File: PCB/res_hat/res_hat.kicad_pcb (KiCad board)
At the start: 2 copper layers, 85 x 56 mm, 55 parts, among them IC1 MCP4725A0T-E_CH, IC2 MCP4725A0T-E_CH, IC3 UCC27324D, J1 Conn_02x20_Odd_Even, J10 Conn_01x02, J11 Jack-DC, J2 Conn_02x04_Odd_Even, J3 Conn_01x03, J4 Conn_01x06, J5 Conn_Coaxial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

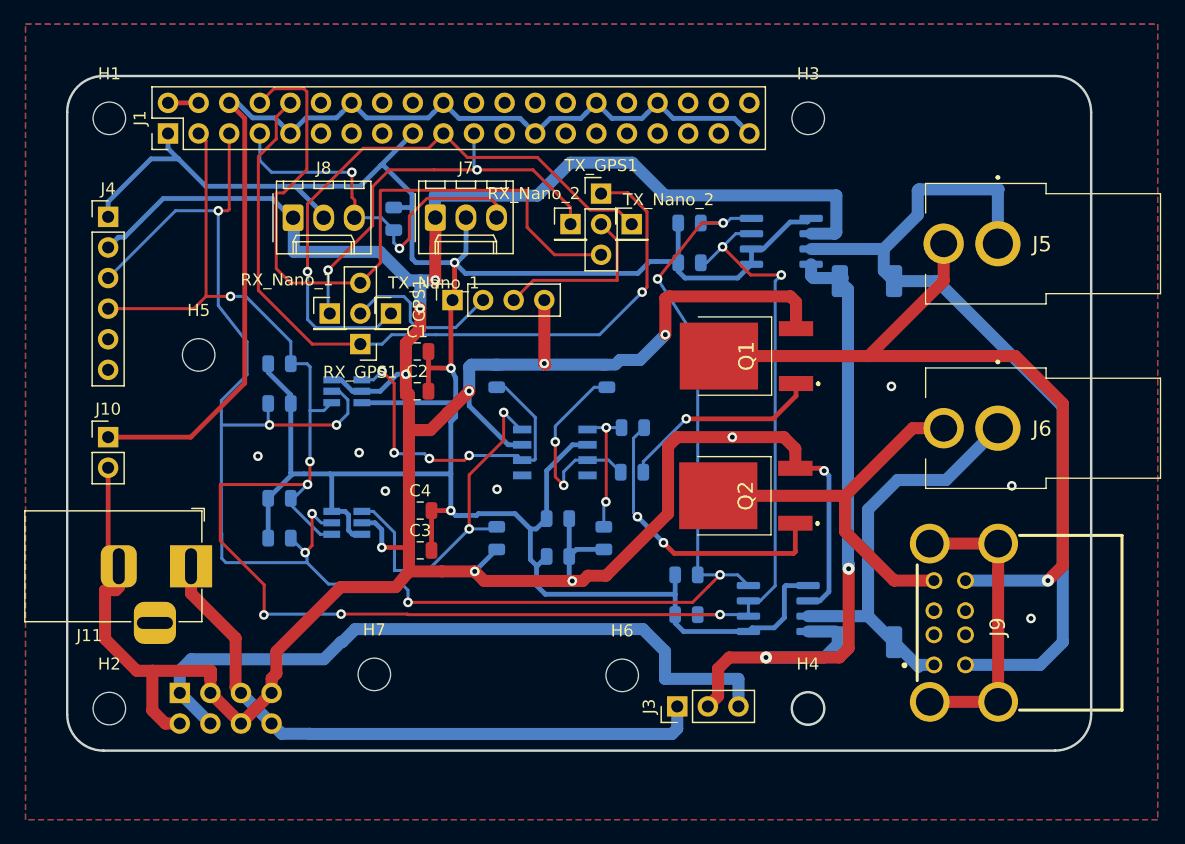
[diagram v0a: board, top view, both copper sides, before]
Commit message: update/add LCSC ref and create fab file
bug for Res_hat with JLCPCB site
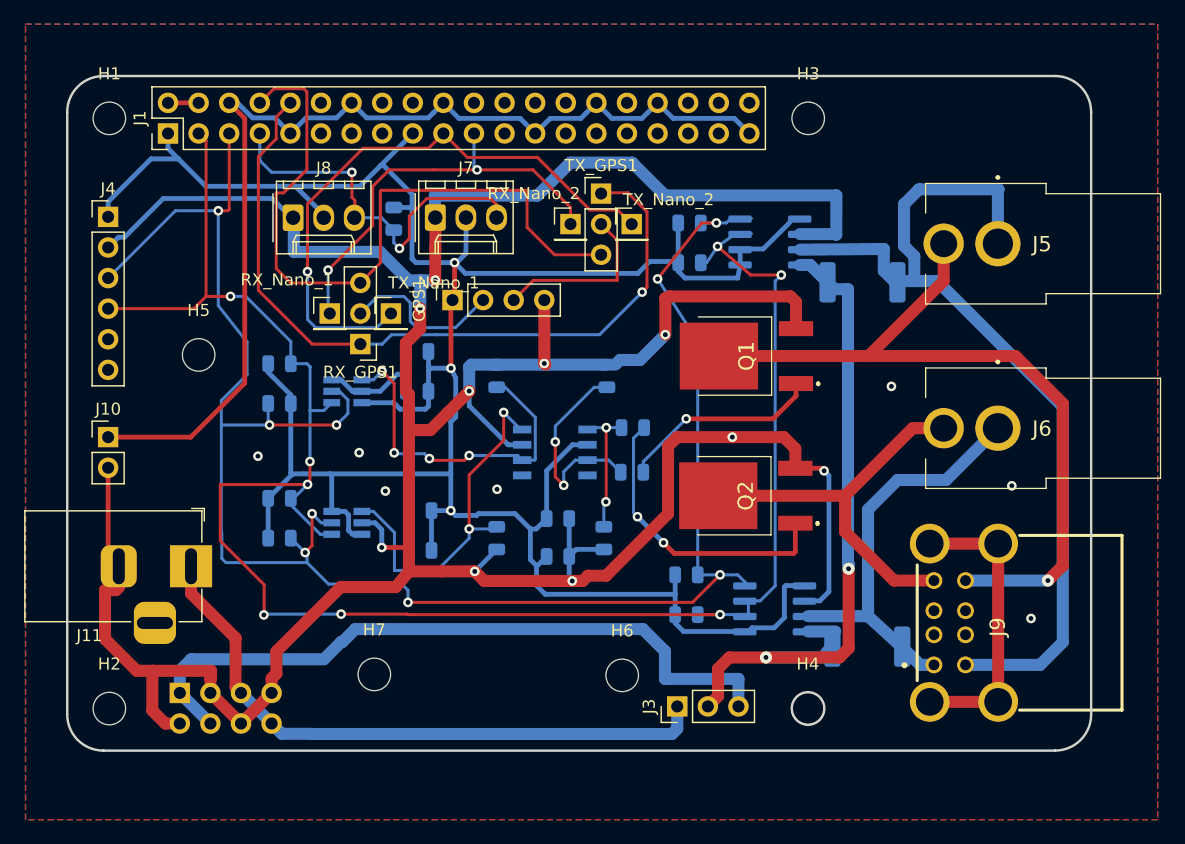
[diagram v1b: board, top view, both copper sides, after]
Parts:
- C1, C2, C3, C4: moved to B.Cu
- R11, R13: value 0.02 -> 0.02 1W; footprint Resistor_SMD:R_2010_5025Metric -> Resistor_SMD:R_2512_6332Metric
- moved U1 0.95 mm to (120.2, 112.1)
- moved R11 0.39 mm to (127.9, 115.4)
- moved R13 0.37 mm to (128.3, 145.7)
- moved U2 0.30 mm to (120.6, 142.5)
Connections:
- IC3 pad 1: (no net) -> Net-(IC3-Pad1)
- IC3 pad 8: (no net) -> Net-(IC3-Pad8)
- J1 pad 11: (no net) -> Net-(J1-Pad11)
- J1 pad 12: (no net) -> Net-(J1-Pad12)
- J1 pad 13: (no net) -> Net-(J1-Pad13)
- J1 pad 15: (no net) -> Net-(J1-Pad15)
- J1 pad 16: (no net) -> Net-(J1-Pad16)
- J1 pad 18: (no net) -> Net-(J1-Pad18)
- J1 pad 22: (no net) -> Net-(J1-Pad22)
- J1 pad 23: (no net) -> Net-(J1-Pad23)
- J1 pad 24: (no net) -> Net-(J1-Pad24)
- J1 pad 26: (no net) -> Net-(J1-Pad26)
- J1 pad 27: (no net) -> Net-(J1-Pad27)
- J1 pad 28: (no net) -> Net-(J1-Pad28)
- J1 pad 29: (no net) -> Net-(J1-Pad29)
- J1 pad 31: (no net) -> Net-(J1-Pad31)
- J1 pad 32: (no net) -> Net-(J1-Pad32)
- J1 pad 33: (no net) -> Net-(J1-Pad33)
- J1 pad 35: (no net) -> Net-(J1-Pad35)
- J1 pad 36: (no net) -> Net-(J1-Pad36)
- J1 pad 37: (no net) -> Net-(J1-Pad37)
- J1 pad 38: (no net) -> Net-(J1-Pad38)
- J1 pad 40: (no net) -> Net-(J1-Pad40)
- J4 pad 5: (no net) -> /CSB
- J4 pad 6: (no net) -> /SDO
- J9 pad 2: (no net) -> Net-(J9-Pad2)
- J9 pad 3: (no net) -> Net-(J9-Pad3)
- J9 pad 6: (no net) -> Net-(J9-Pad6)
- J9 pad 7: (no net) -> Net-(J9-Pad7)
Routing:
- net +3V3: track 226.1 -> 221.6 mm
- net Net-(J5-Pad1): track 73.1 -> 76.3 mm
- net GND: track 299.1 -> 300.2 mm, vias 18 -> 17
- net /SCL: track 159.5 -> 158.9 mm
- net VD: track 58.4 -> 57.9 mm

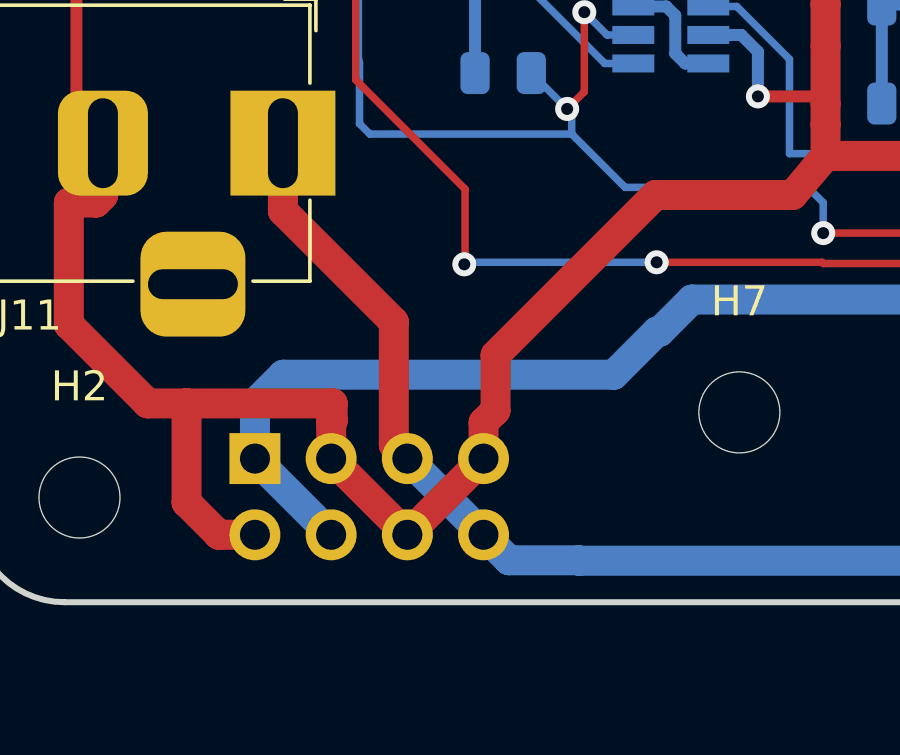
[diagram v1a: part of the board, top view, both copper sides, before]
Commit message: correct wring align for 4x2pin connector
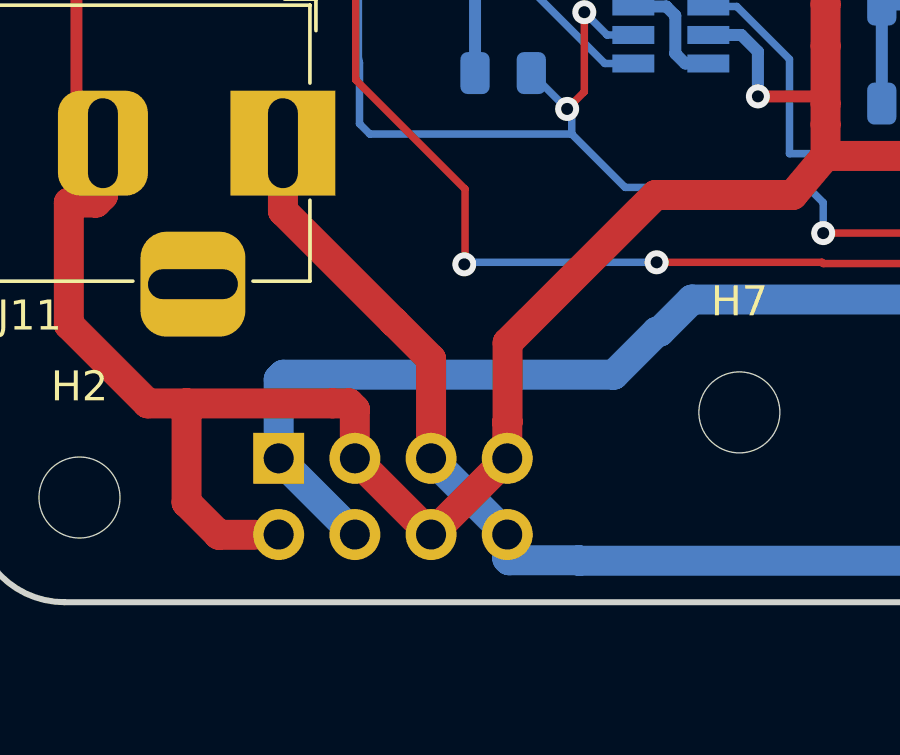
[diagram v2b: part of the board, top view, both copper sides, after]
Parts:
- moved J2 0.79 mm to (72.0, 149.5)
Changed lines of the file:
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@@
-(kicad_pcb (version 20171130) (host pcbnew 5.1.6-c6e7f7d~87~ubuntu18.04.1)
+(kicad_pcb (version 20171130) (host pcbnew "(5.1.5)-3")
   (general
     (thickness 1.6)
     (drawings 9)
-    (tracks 675)
+    (tracks 677)
     (zones 0)
     (modules 55)
@@
   )
   (module Connector_PinHeader_2.54mm:PinHeader_2x04_P2.54mm_Vertical (layer B.Cu)
-    (at 71.228 149.5023 270)
+    (at 72.01916 149.49424 270)
     (descr "Through hole straight pin header, 2x04, 2.54mm pitch, double rows")
     (tags "Through hole pin header THT 2x04 2.54mm double row")
@@
   (segment (start 65.278 130.81) (end 65.278 138.1054) (width 0.4) (layer F.Cu) (net 5))
   (segment (start 84.582 140.716) (end 89.154 140.716) (width 1) (layer F.Cu) (net 5))
-  (segment (start 79.248 146.05) (end 84.582 140.716) (width 1) (layer F.Cu) (net 5))
   (segment (start 89.154 140.716) (end 90.2485 139.413881) (width 1) (layer F.Cu) (net 5))
   (segment (start 92.996119 139.413881) (end 95.711619 139.413881) (width 1) (layer F.Cu) (net 5))
   (via (at 103.8075 140.208) (size 0.8) (drill 0.4) (layers F.Cu B.Cu) (net 5))
-  (segment (start 79.248 147.900219) (end 79.248 146.05) (width 1) (layer F.Cu) (net 5))
-  (segment (start 78.848 148.300219) (end 79.248 147.900219) (width 1) (layer F.Cu) (net 5))
-  (segment (start 78.848 149.5023) (end 78.848 148.300219) (width 1) (layer F.Cu) (net 5))
   (segment (start 66.1614 140.7388) (end 66.1614 138.9888) (width 1) (layer F.Cu) (net 5))
   (segment (start 65.024 140.97) (end 65.9302 140.97) (width 1) (layer F.Cu) (net 5))
   (segment (start 65.024 145.034) (end 65.024 140.97) (width 1) (layer F.Cu) (net 5))
-  (segment (start 73.768 149.5023) (end 73.768 148.300219) (width 1) (layer F.Cu) (net 5))
   (segment (start 67.652299 147.662299) (end 65.024 145.034) (width 1) (layer F.Cu) (net 5))
   (segment (start 65.9302 140.97) (end 66.1614 140.7388) (width 1) (layer F.Cu) (net 5))
-  (segment (start 73.768 148.300219) (end 73.82008 148.248139) (width 1) (layer F.Cu) (net 5))
-  (segment (start 73.82008 148.248139) (end 73.82008 147.662299) (width 1) (layer F.Cu) (net 5))
   (segment (start 70.025919 152.0423) (end 71.228 152.0423) (width 1) (layer F.Cu) (net 5))
   (segment (start 68.947699 147.662299) (end 68.947699 150.96408) (width 1) (layer F.Cu) (net 5))
@@
   (segment (start 68.947699 150.96408) (end 70.025919 152.0423) (width 1) (layer F.Cu) (net 5))
   (segment (start 73.82008 147.662299) (end 68.947699 147.662299) (width 1) (layer F.Cu) (net 5))
-  (segment (start 73.768 149.5023) (end 76.308 152.0423) (width 1) (layer F.Cu) (net 5))
-  (segment (start 78.848 149.5023) (end 76.308 152.0423) (width 1) (layer F.Cu) (net 5))
   (segment (start 92.43568 112.62632) (end 92.46616 110.39856) (width 1) (layer F.Cu) (net 5))
   (segment (start 107.38 122.2525) (end 107.77092 121.86158) (width 1) (layer B.Cu) (net 5))
@@
   (segment (start 100.91166 108.21924) (end 103.64978 105.48112) (width 1) (layer B.Cu) (net 5))
   (segment (start 111.506 108.204) (end 125.73 108.204) (width 1) (layer B.Cu) (net 5))
+  (segment (start 73.82008 147.662299) (end 74.360439 147.662299) (width 1) (layer F.Cu) (net 5))
+  (segment (start 74.55916 147.86102) (end 74.55916 149.49424) (width 1) (layer F.Cu) (net 5))
+  (segment (start 74.360439 147.662299) (end 74.55916 147.86102) (width 1) (layer F.Cu) (net 5))
+  (segment (start 79.63916 148.292159) (end 79.64932 148.281999) (width 1) (layer F.Cu) (net 5))
+  (segment (start 79.64932 148.281999) (end 79.64932 145.64106) (width 1) (layer F.Cu) (net 5))
+  (segment (start 79.63916 149.49424) (end 79.63916 148.292159) (width 1) (layer F.Cu) (net 5))
+  (segment (start 79.64932 145.64106) (end 84.582 140.716) (width 1) (layer F.Cu) (net 5))
+  (segment (start 77.09916 152.03424) (end 79.63916 149.49424) (width 1) (layer F.Cu) (net 5))
+  (segment (start 74.55916 149.49424) (end 77.09916 152.03424) (width 1) (layer F.Cu) (net 5))
   (segment (start 117.74678 112.63122) (end 117.74678 113.90122) (width 0.4) (layer B.Cu) (net 6))
   (segment (start 119.658 112.649) (end 118.683 112.649) (width 0.4) (layer B.Cu) (net 6))
@@
   (segment (start 112.086 152.908) (end 112.522 152.472) (width 1) (layer B.Cu) (net 15))
   (segment (start 82.042 152.908) (end 112.086 152.908) (width 1) (layer B.Cu) (net 15))
-  (segment (start 75.858001 144.946001) (end 75.858001 149.052301) (width 1) (layer F.Cu) (net 15))
   (segment (start 72.1614 138.9888) (end 72.1614 141.2494) (width 1) (layer F.Cu) (net 15))
-  (segment (start 75.858001 149.052301) (end 76.308 149.5023) (width 1) (layer F.Cu) (net 15))
   (segment (start 72.1614 141.2494) (end 75.858001 144.946001) (width 1) (layer F.Cu) (net 15))
-  (segment (start 76.308 149.5023) (end 78.848 152.0423) (width 1) (layer B.Cu) (net 15))
   (segment (start 82.026299 152.892299) (end 82.042 152.908) (width 1) (layer B.Cu) (net 15))
   (segment (start 79.697999 152.892299) (end 82.026299 152.892299) (width 1) (layer B.Cu) (net 15))
-  (segment (start 78.848 152.0423) (end 79.697999 152.892299) (width 1) (layer B.Cu) (net 15))
-  (segment (start 71.228 149.5023) (end 73.768 152.0423) (width 1) (layer B.Cu) (net 16))
+  (segment (start 75.858001 144.946001) (end 75.863081 144.946001) (width 1) (layer F.Cu) (net 15))
+  (segment (start 77.09916 146.18208) (end 77.09916 149.49424) (width 1) (layer F.Cu) (net 15))
+  (segment (start 75.863081 144.946001) (end 77.09916 146.18208) (width 1) (layer F.Cu) (net 15))
+  (segment (start 79.63916 152.83346) (end 79.697999 152.892299) (width 1) (layer B.Cu) (net 15))
+  (segment (start 79.63916 152.03424) (end 79.63916 152.83346) (width 1) (layer B.Cu) (net 15))
+  (segment (start 77.09916 149.49424) (end 79.63916 152.03424) (width 1) (layer B.Cu) (net 15))
   (segment (start 117.602 148.336) (end 117.602 150.622) (width 1) (layer B.Cu) (net 16))
   (segment (start 109.6645 144.20088) (end 111.506 146.04238) (width 1) (layer B.Cu) (net 16))
   (segment (start 85.79358 144.20088) (end 109.6645 144.20088) (width 1) (layer B.Cu) (net 16))
-  (segment (start 71.228 147.6523) (end 72.17415 146.70615) (width 1) (layer B.Cu) (net 16))
   (segment (start 72.17415 146.70615) (end 83.18925 146.70615) (width 1) (layer B.Cu) (net 16))
-  (segment (start 71.228 149.5023) (end 71.228 147.6523) (width 1) (layer B.Cu) (net 16))
   (segment (start 83.18925 146.70615) (end 84.62518 145.27022) (width 1) (layer B.Cu) (net 16))
   (segment (start 84.62518 145.27022) (end 84.72424 145.27022) (width 1) (layer B.Cu) (net 16))
@@
   (segment (start 111.506 146.04238) (end 111.506 148.336) (width 1) (layer B.Cu) (net 16))
   (segment (start 84.72424 145.27022) (end 85.79358 144.20088) (width 1) (layer B.Cu) (net 16))
+  (segment (start 72.01916 146.86114) (end 72.01916 149.49424) (width 1) (layer B.Cu) (net 16))
+  (segment (start 72.17415 146.70615) (end 72.01916 146.86114) (width 1) (layer B.Cu) (net 16))
+  (segment (start 72.01916 149.49424) (end 74.55916 152.03424) (width 1) (layer B.Cu) (net 16))
   (segment (start 97.282 109.982) (end 97.51568 110.17632) (width 0.25) (layer F.Cu) (net 17))
   (segment (start 85.75802 108.6066) (end 85.52052 108.3691) (width 0.25) (layer F.Cu) (net 17))
